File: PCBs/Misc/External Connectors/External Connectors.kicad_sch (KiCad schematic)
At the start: 8 parts, among them J1 Conn_02x04_Top_Bottom, J2 Conn_02x04_Top_Bottom, J3 USB_B, J4 USB_A

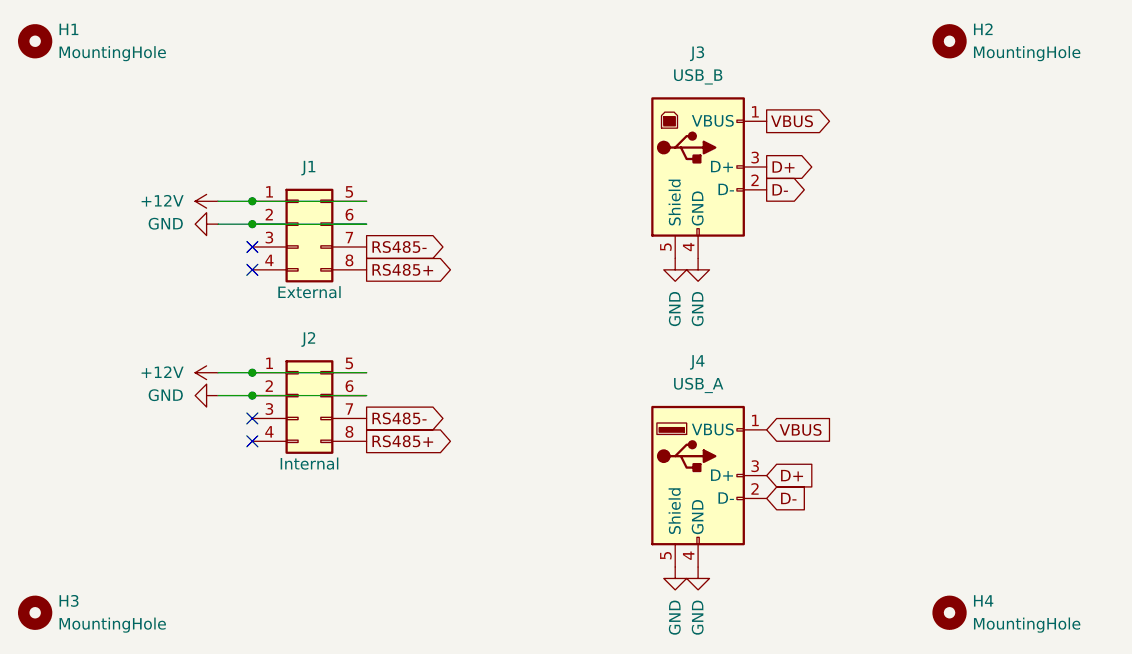
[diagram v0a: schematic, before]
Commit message: Updated hub pinout for more power
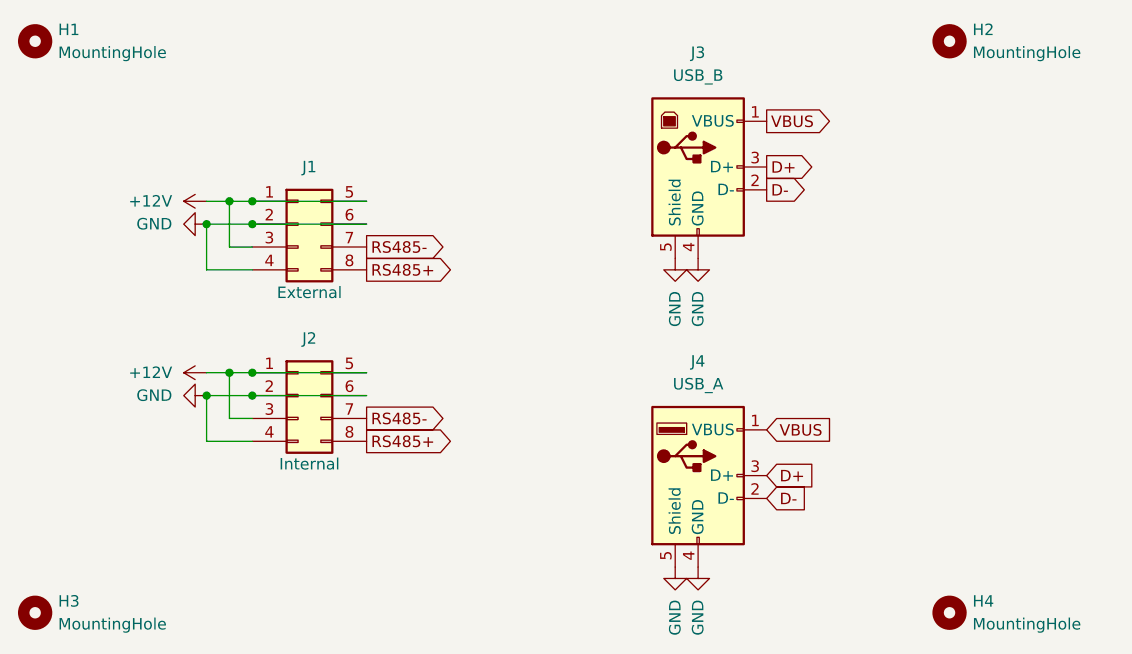
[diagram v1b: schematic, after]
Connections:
- net +12V: now also J1.3 (Pin_3), J2.3 (Pin_3)
- net GND: now also J1.4 (Pin_4), J2.4 (Pin_4)
- no-connect marks 4 -> 0
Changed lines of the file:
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@@
   (junction (at 125.73 81.28) (diameter 0) (color 0 0 0 0)
   )
+  (junction (at 120.65 102.87) (diameter 0) (color 0 0 0 0)
+  )
   (junction (at 125.73 102.87) (diameter 0) (color 0 0 0 0)
   )
   (junction (at 125.73 83.82) (diameter 0) (color 0 0 0 0)
   )
-  (no_connect (at 125.73 88.9))
-  (no_connect (at 125.73 86.36))
-  (no_connect (at 125.73 107.95))
-  (no_connect (at 125.73 105.41))
+  (junction (at 120.65 83.82) (diameter 0) (color 0 0 0 0)
+  )
+  (junction (at 123.19 100.33) (diameter 0) (color 0 0 0 0)
+  )
+  (junction (at 123.19 81.28) (diameter 0) (color 0 0 0 0)
+  )
   (wire (pts (xy 125.73 100.33) (xy 138.43 100.33))
     (stroke (width 0) (type default) (color 0 0 0 0))
   )
+  (wire (pts (xy 123.19 86.36) (xy 123.19 81.28))
+    (stroke (width 0) (type default) (color 0 0 0 0))
+  )
+  (wire (pts (xy 120.65 88.9) (xy 120.65 83.82))
+    (stroke (width 0) (type default) (color 0 0 0 0))
+  )
   (wire (pts (xy 125.73 102.87) (xy 138.43 102.87))
     (stroke (width 0) (type default) (color 0 0 0 0))
   )
-  (wire (pts (xy 121.92 100.33) (xy 125.73 100.33))
-    (stroke (width 0) (type default) (color 0 0 0 0))
-  )
-  (wire (pts (xy 121.92 83.82) (xy 125.73 83.82))
+  (wire (pts (xy 123.19 100.33) (xy 125.73 100.33))
+    (stroke (width 0) (type default) (color 0 0 0 0))
+  )
+  (wire (pts (xy 120.65 102.87) (xy 120.65 107.95))
+    (stroke (width 0) (type default) (color 0 0 0 0))
+  )
+  (wire (pts (xy 125.73 88.9) (xy 120.65 88.9))
+    (stroke (width 0) (type default) (color 0 0 0 0))
+  )
+  (wire (pts (xy 125.73 86.36) (xy 123.19 86.36))
+    (stroke (width 0) (type default) (color 0 0 0 0))
+  )
+  (wire (pts (xy 120.65 100.33) (xy 123.19 100.33))
+    (stroke (width 0) (type default) (color 0 0 0 0))
+  )
+  (wire (pts (xy 120.65 83.82) (xy 125.73 83.82))
     (stroke (width 0) (type default) (color 0 0 0 0))
   )
@@
     (stroke (width 0) (type default) (color 0 0 0 0))
   )
-  (wire (pts (xy 121.92 81.28) (xy 125.73 81.28))
+  (wire (pts (xy 120.65 107.95) (xy 125.73 107.95))
+    (stroke (width 0) (type default) (color 0 0 0 0))
+  )
+  (wire (pts (xy 120.65 81.28) (xy 123.19 81.28))
+    (stroke (width 0) (type default) (color 0 0 0 0))
+  )
+  (wire (pts (xy 123.19 105.41) (xy 123.19 100.33))
+    (stroke (width 0) (type default) (color 0 0 0 0))
+  )
+  (wire (pts (xy 123.19 81.28) (xy 125.73 81.28))
+    (stroke (width 0) (type default) (color 0 0 0 0))
+  )
+  (wire (pts (xy 125.73 105.41) (xy 123.19 105.41))
     (stroke (width 0) (type default) (color 0 0 0 0))
   )
@@
     (stroke (width 0) (type default) (color 0 0 0 0))
   )
-  (wire (pts (xy 121.92 102.87) (xy 125.73 102.87))
+  (wire (pts (xy 120.65 102.87) (xy 125.73 102.87))
     (stroke (width 0) (type default) (color 0 0 0 0))
   )
@@
     )
   )
-  (symbol (lib_id "power:GND") (at 121.92 83.82 270) (unit 1)
-    (in_bom yes) (on_board yes) (fields_autoplaced)
-    (property "Reference" "#PWR0103" (id 0) (at 115.57 83.82 0)
-      (effects (font (size 1.27 1.27)) hide)
-    )
-    (property "Value" "GND" (id 1) (at 118.11 83.8199 90)
+  (symbol (lib_id "power:GND") (at 120.65 83.82 270) (unit 1)
+    (in_bom yes) (on_board yes) (fields_autoplaced)
+    (property "Reference" "#PWR0103" (id 0) (at 114.3 83.82 0)
+      (effects (font (size 1.27 1.27)) hide)
+    )
+    (property "Value" "GND" (id 1) (at 116.84 83.8199 90)
       (effects (font (size 1.27 1.27)) (justify right))
     )
-    (property "Footprint" "" (id 2) (at 121.92 83.82 0)
-      (effects (font (size 1.27 1.27)) hide)
-    )
-    (property "Datasheet" "" (id 3) (at 121.92 83.82 0)
+    (property "Footprint" "" (id 2) (at 120.65 83.82 0)
+      (effects (font (size 1.27 1.27)) hide)
+    )
+    (property "Datasheet" "" (id 3) (at 120.65 83.82 0)
       (effects (font (size 1.27 1.27)) hide)
     )
@@
     (pin "5")
   )
-  (symbol (lib_id "power:+12V") (at 121.92 100.33 90) (unit 1)
-    (in_bom yes) (on_board yes) (fields_autoplaced)
-    (property "Reference" "#PWR0101" (id 0) (at 125.73 100.33 0)
-      (effects (font (size 1.27 1.27)) hide)
-    )
-    (property "Value" "+12V" (id 1) (at 118.11 100.3299 90)
-      (effects (font (size 1.27 1.27)) (justify left))
-    )
-    (property "Footprint" "" (id 2) (at 121.92 100.33 0)
-      (effects (font (size 1.27 1.27)) hide)
-    )
-    (property "Datasheet" "" (id 3) (at 121.92 100.33 0)
-      (effects (font (size 1.27 1.27)) hide)
-    )
-    (pin "1")
-  )
-  (symbol (lib_id "power:GND") (at 121.92 102.87 270) (unit 1)
-    (in_bom yes) (on_board yes) (fields_autoplaced)
-    (property "Reference" "#PWR0102" (id 0) (at 115.57 102.87 0)
-      (effects (font (size 1.27 1.27)) hide)
-    )
-    (property "Value" "GND" (id 1) (at 118.11 102.8699 90)
+  (symbol (lib_id "power:+12V") (at 120.65 100.33 90) (unit 1)
+    (in_bom yes) (on_board yes) (fields_autoplaced)
+    (property "Reference" "#PWR0101" (id 0) (at 124.46 100.33 0)
+      (effects (font (size 1.27 1.27)) hide)
+    )
+    (property "Value" "+12V" (id 1) (at 116.84 100.3299 90)
+      (effects (font (size 1.27 1.27)) (justify left))
+    )
+    (property "Footprint" "" (id 2) (at 120.65 100.33 0)
+      (effects (font (size 1.27 1.27)) hide)
+    )
+    (property "Datasheet" "" (id 3) (at 120.65 100.33 0)
+      (effects (font (size 1.27 1.27)) hide)
+    )
+    (pin "1")
+  )
+  (symbol (lib_id "power:GND") (at 120.65 102.87 270) (unit 1)
+    (in_bom yes) (on_board yes) (fields_autoplaced)
+    (property "Reference" "#PWR0102" (id 0) (at 114.3 102.87 0)
+      (effects (font (size 1.27 1.27)) hide)
+    )
+    (property "Value" "GND" (id 1) (at 116.84 102.8699 90)
       (effects (font (size 1.27 1.27)) (justify right))
     )
-    (property "Footprint" "" (id 2) (at 121.92 102.87 0)
-      (effects (font (size 1.27 1.27)) hide)
-    )
-    (property "Datasheet" "" (id 3) (at 121.92 102.87 0)
+    (property "Footprint" "" (id 2) (at 120.65 102.87 0)
+      (effects (font (size 1.27 1.27)) hide)
+    )
+    (property "Datasheet" "" (id 3) (at 120.65 102.87 0)
       (effects (font (size 1.27 1.27)) hide)
     )
@@
     (pin "8")
   )
-  (symbol (lib_id "power:+12V") (at 121.92 81.28 90) (unit 1)
-    (in_bom yes) (on_board yes) (fields_autoplaced)
-    (property "Reference" "#PWR0104" (id 0) (at 125.73 81.28 0)
-      (effects (font (size 1.27 1.27)) hide)
-    )
-    (property "Value" "+12V" (id 1) (at 118.11 81.2799 90)
-      (effects (font (size 1.27 1.27)) (justify left))
-    )
-    (property "Footprint" "" (id 2) (at 121.92 81.28 0)
-      (effects (font (size 1.27 1.27)) hide)
-    )
-    (property "Datasheet" "" (id 3) (at 121.92 81.28 0)
-      (effects (font (size 1.27 1.27)) hide)
-    )
+  (symbol (lib_id "power:+12V") (at 120.65 81.28 90) (unit 1)
+    (in_bom yes) (on_board yes) (fields_autoplaced)
+    (property "Reference" "#PWR0104" (id 0) (at 124.46 81.28 0)
+      (effects (font (size 1.27 1.27)) hide)
+    )
+    (property "Value" "+12V" (id 1) (at 116.84 81.2799 90)
+      (effects (font (size 1.27 1.27)) (justify left))
+    )
+    (property "Footprint" "" (id 2) (at 120.65 81.28 0)
+      (effects (font (size 1.27 1.27)) hide)
+    )
+    (property "Datasheet" "" (id 3) (at 120.65 81.28 0)
+      (effects (font (size 1.27 1.27)) hide)
+    )
